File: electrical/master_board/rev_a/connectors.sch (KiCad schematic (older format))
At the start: 9 parts, among them CN3 LIDAR_ADAPTER;2xF1x2, CN40 MIKROBUS_MATE;SMALL, CN41 MIKROBUS_MATE;MEDIUM, U10 SN74HCS595;TTSOP16, U11 SN74HCS166;TTSOP16, U12 SN74HCS166;TTSOP16

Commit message: Reannoted. Postioned components are in the 80-99 reference range.
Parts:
- renumbered C18 to C14, C19 to C15, C20 to C16, CN3 to CN5, CN40 to CN88, CN41 to CN89, U10 to U5, U11 to U6, U12 to U7
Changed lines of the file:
@@
 P 4500 4100
 AR Path="/5F4CFB97" Ref="CN?"  Part="1"
-AR Path="/5F4CEE66/5F4CFB97" Ref="CN40"  Part="1"
-F 0 "CN40" H 4800 4250 50  0000 C CNN
+AR Path="/5F4CEE66/5F4CFB97" Ref="CN88"  Part="1"
+F 0 "CN88" H 4800 4250 50  0000 C CNN
 F 1 "MIKROBUS_MATE;SMALL" H 5050 2850 50  0000 C CNN
 F 2 "HR2:MIKROBUS_SMALL_MATE" H 4700 4150 60  0001 L CNN
@@
 P 4500 2500
 AR Path="/5F4CFB9E" Ref="CN?"  Part="1"
-AR Path="/5F4CEE66/5F4CFB9E" Ref="CN41"  Part="1"
-F 0 "CN41" H 4800 2650 50  0000 C CNN
+AR Path="/5F4CEE66/5F4CFB9E" Ref="CN89"  Part="1"
+F 0 "CN89" H 4800 2650 50  0000 C CNN
 F 1 "MIKROBUS_MATE;MEDIUM" H 5050 1250 50  0000 C CNN
 F 2 "HR2:MIKROBUS_MEDIUM_MATE" H 4700 2550 60  0001 L CNN
@@
 ~DIO_NSS
 $Comp
-L HR2:SN74HCS595;TTSOP16 U10
+L HR2:SN74HCS595;TTSOP16 U5
 U 1 1 5FD710B8
 P 2800 6400
-F 0 "U10" H 3050 6550 50  0000 C CNN
+F 0 "U5" H 3050 6550 50  0000 C CNN
 F 1 "SN74HCS595;TTSOP16" H 3300 5250 50  0000 C CNN
 F 2 "Package_SO:TSSOP-16_4.4x5mm_P0.65mm" H 3000 6450 60  0001 L CNN
@@
 P 4600 5700
 AR Path="/5F4A826A/5F84DF13" Ref="CN?"  Part="1"
-AR Path="/5F4CEE66/5F84DF13" Ref="CN3"  Part="1"
-F 0 "CN3" H 4850 5850 50  0000 C CNN
+AR Path="/5F4CEE66/5F84DF13" Ref="CN5"  Part="1"
+F 0 "CN5" H 4850 5850 50  0000 C CNN
 F 1 "LIDAR_ADAPTER;2xF1x2" H 5100 5150 50  0000 C CNN
 F 2 "HR2:LIDAR_ADAPTER_2xF1x2" H 4800 5750 60  0001 L CNN
@@
 	5900 5500 6000 5600
 $Comp
-L HR2:SN74HCS166;TTSOP16 U11
+L HR2:SN74HCS166;TTSOP16 U6
 U 1 1 5F845F8F
 P 8300 2500
-F 0 "U11" H 8550 2650 60  0000 C CNN
+F 0 "U6" H 8550 2650 60  0000 C CNN
 F 1 "SN74HCS166;TTSOP16" H 8900 1150 60  0000 C CNN
 F 2 "Package_SO:TSSOP-16_4.4x5mm_P0.65mm" H 8500 2550 60  0001 L CNN
@@
 $EndComp
 $Comp
-L HR2:SN74HCS166;TTSOP16 U12
+L HR2:SN74HCS166;TTSOP16 U7
 U 1 1 5F849624
 P 8300 4700
-F 0 "U12" H 8550 4850 60  0000 C CNN
+F 0 "U7" H 8550 4850 60  0000 C CNN
 F 1 "SN74HCS166;TTSOP16" H 8900 3350 60  0000 C CNN
 F 2 "Package_SO:TSSOP-16_4.4x5mm_P0.65mm" H 8500 4750 60  0001 L CNN
@@
 P 4600 1750
 AR Path="/5F48CAAD/5F97D822" Ref="C?"  Part="1"
-AR Path="/5F4CEE66/5F97D822" Ref="C18"  Part="1"
-F 0 "C18" H 4400 1850 50  0000 L CNN
+AR Path="/5F4CEE66/5F97D822" Ref="C14"  Part="1"
+F 0 "C14" H 4400 1850 50  0000 L CNN
 F 1 "10pF;1608" H 4650 1650 50  0000 L CNN
 F 2 "" H 4638 1600 50  0001 C CNN
@@
 P 5200 1750
 AR Path="/5F48CAAD/5F97D82E" Ref="C?"  Part="1"
-AR Path="/5F4CEE66/5F97D82E" Ref="C19"  Part="1"
-F 0 "C19" H 5000 1850 50  0000 L CNN
+AR Path="/5F4CEE66/5F97D82E" Ref="C15"  Part="1"
+F 0 "C15" H 5000 1850 50  0000 L CNN
 F 1 "10pF;1608" H 5250 1650 50  0000 L CNN
 F 2 "" H 5238 1600 50  0001 C CNN
@@
 P 5800 1750
 AR Path="/5F48CAAD/5F97D834" Ref="C?"  Part="1"
-AR Path="/5F4CEE66/5F97D834" Ref="C20"  Part="1"
-F 0 "C20" H 5600 1850 50  0000 L CNN
+AR Path="/5F4CEE66/5F97D834" Ref="C16"  Part="1"
+F 0 "C16" H 5600 1850 50  0000 L CNN
 F 1 "10pF;1608" H 5850 1650 50  0000 L CNN
 F 2 "" H 5838 1600 50  0001 C CNN

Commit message: Assigned PCB footprints.
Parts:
- C14, C15, C16: footprint (none) -> Capacitor_SMD:C_0603_1608Metric
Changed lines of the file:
@@
 F 0 "C14" H 4400 1850 50  0000 L CNN
 F 1 "10pF;1608" H 4650 1650 50  0000 L CNN
-F 2 "" H 4638 1600 50  0001 C CNN
+F 2 "Capacitor_SMD:C_0603_1608Metric" H 4638 1600 50  0001 C CNN
 F 3 "~" H 4600 1750 50  0001 C CNN
 	1    4600 1750
@@
 F 0 "C15" H 5000 1850 50  0000 L CNN
 F 1 "10pF;1608" H 5250 1650 50  0000 L CNN
-F 2 "" H 5238 1600 50  0001 C CNN
+F 2 "Capacitor_SMD:C_0603_1608Metric" H 5238 1600 50  0001 C CNN
 F 3 "~" H 5200 1750 50  0001 C CNN
 	1    5200 1750
@@
 F 0 "C16" H 5600 1850 50  0000 L CNN
 F 1 "10pF;1608" H 5850 1650 50  0000 L CNN
-F 2 "" H 5838 1600 50  0001 C CNN
+F 2 "Capacitor_SMD:C_0603_1608Metric" H 5838 1600 50  0001 C CNN
 F 3 "~" H 5800 1750 50  0001 C CNN
 	1    5800 1750

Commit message: Imported footprints to PCB.
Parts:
- CN5: footprint HR2:LIDAR_ADAPTER_2xF1x2 -> HR2:LIDAR_ADAPTER_2xF1x2+Fx3
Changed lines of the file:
@@
 F 0 "CN5" H 4850 5850 50  0000 C CNN
 F 1 "LIDAR_ADAPTER;2xF1x2" H 5100 5150 50  0000 C CNN
-F 2 "HR2:LIDAR_ADAPTER_2xF1x2" H 4800 5750 60  0001 L CNN
+F 2 "HR2:LIDAR_ADAPTER_2xF1x2+Fx3" H 4800 5750 60  0001 L CNN
 F 3 "Lidar Adapter Connectors" H 4800 5550 60  0001 L CNN
 F 4 "Lidar Adapter Connectors" H 4800 5650 60  0001 L CNN "manf#"

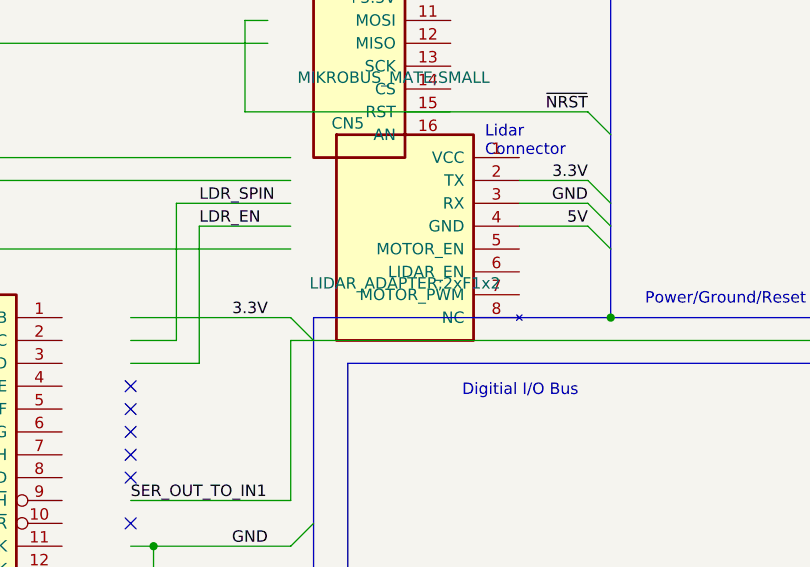
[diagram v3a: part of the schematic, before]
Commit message: Postioned all the components properly.
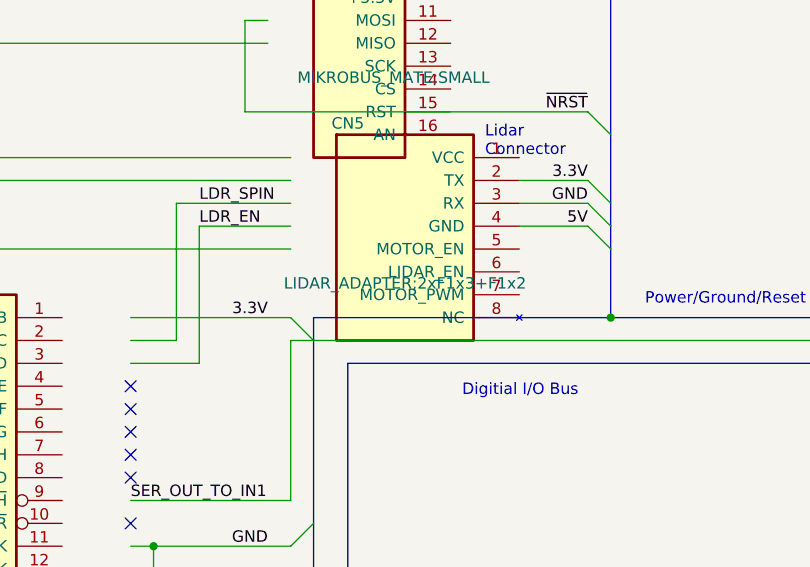
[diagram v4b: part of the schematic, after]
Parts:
- CN5: value LIDAR_ADAPTER;2xF1x2 -> LIDAR_ADAPTER;2xF1x3+F1x2; footprint HR2:LIDAR_ADAPTER_2xF1x2+Fx3 -> HR2:LIDAR_ADAPTER_2xF1x3+F1x2
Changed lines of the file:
@@
 AR Path="/5F4CEE66/5F84DF13" Ref="CN5"  Part="1"
 F 0 "CN5" H 4850 5850 50  0000 C CNN
-F 1 "LIDAR_ADAPTER;2xF1x2" H 5100 5150 50  0000 C CNN
-F 2 "HR2:LIDAR_ADAPTER_2xF1x2+Fx3" H 4800 5750 60  0001 L CNN
+F 1 "LIDAR_ADAPTER;2xF1x3+F1x2" H 5100 5150 50  0000 C CNN
+F 2 "HR2:LIDAR_ADAPTER_2xF1x3+F1x2" H 4800 5750 60  0001 L CNN
 F 3 "Lidar Adapter Connectors" H 4800 5550 60  0001 L CNN
 F 4 "Lidar Adapter Connectors" H 4800 5650 60  0001 L CNN "manf#"

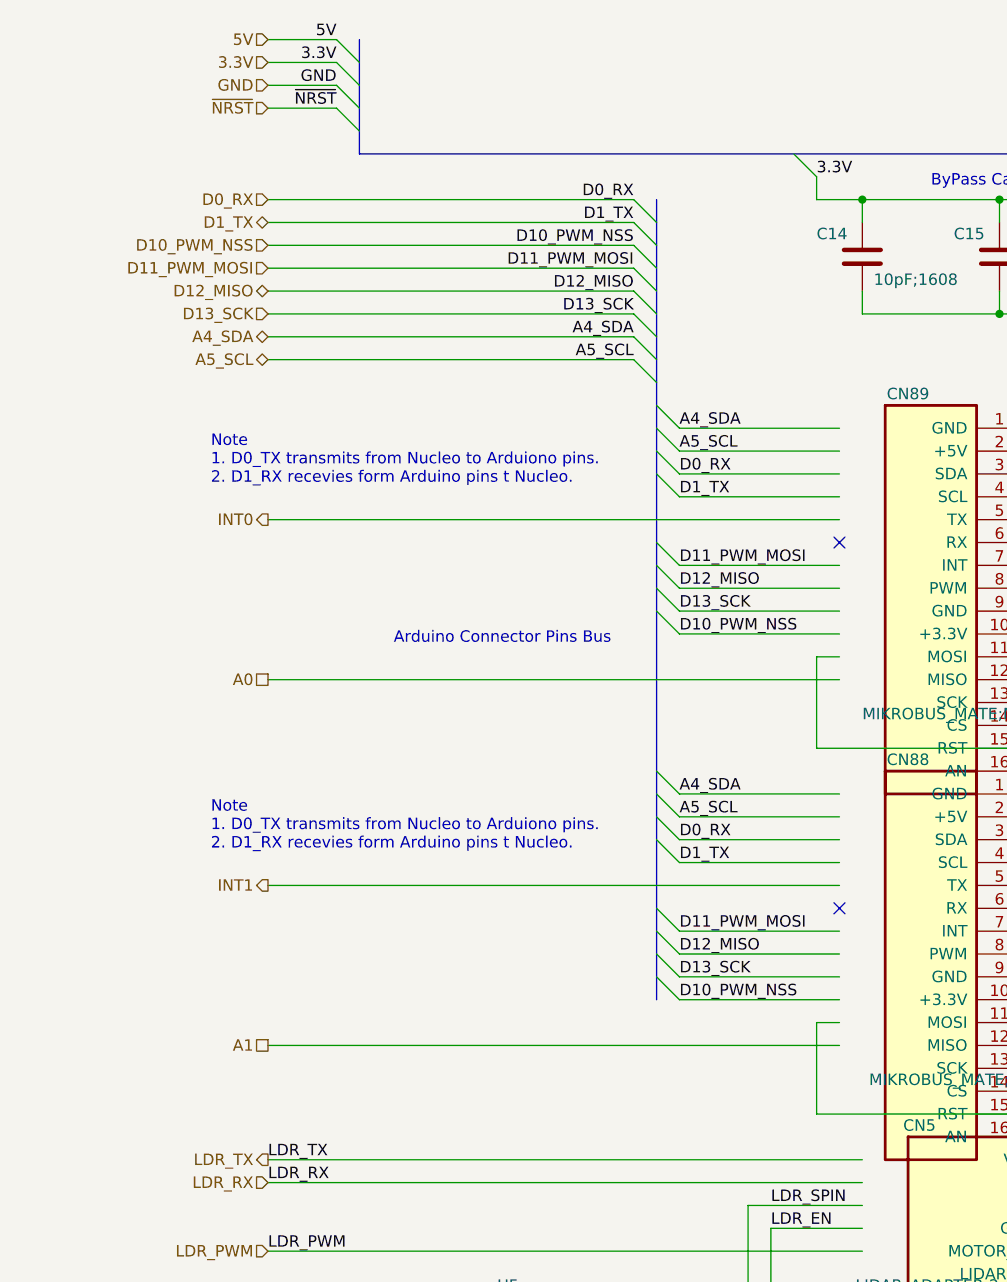
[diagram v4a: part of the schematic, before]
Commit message: Weaving traces from NE corner around the heat sink holes.
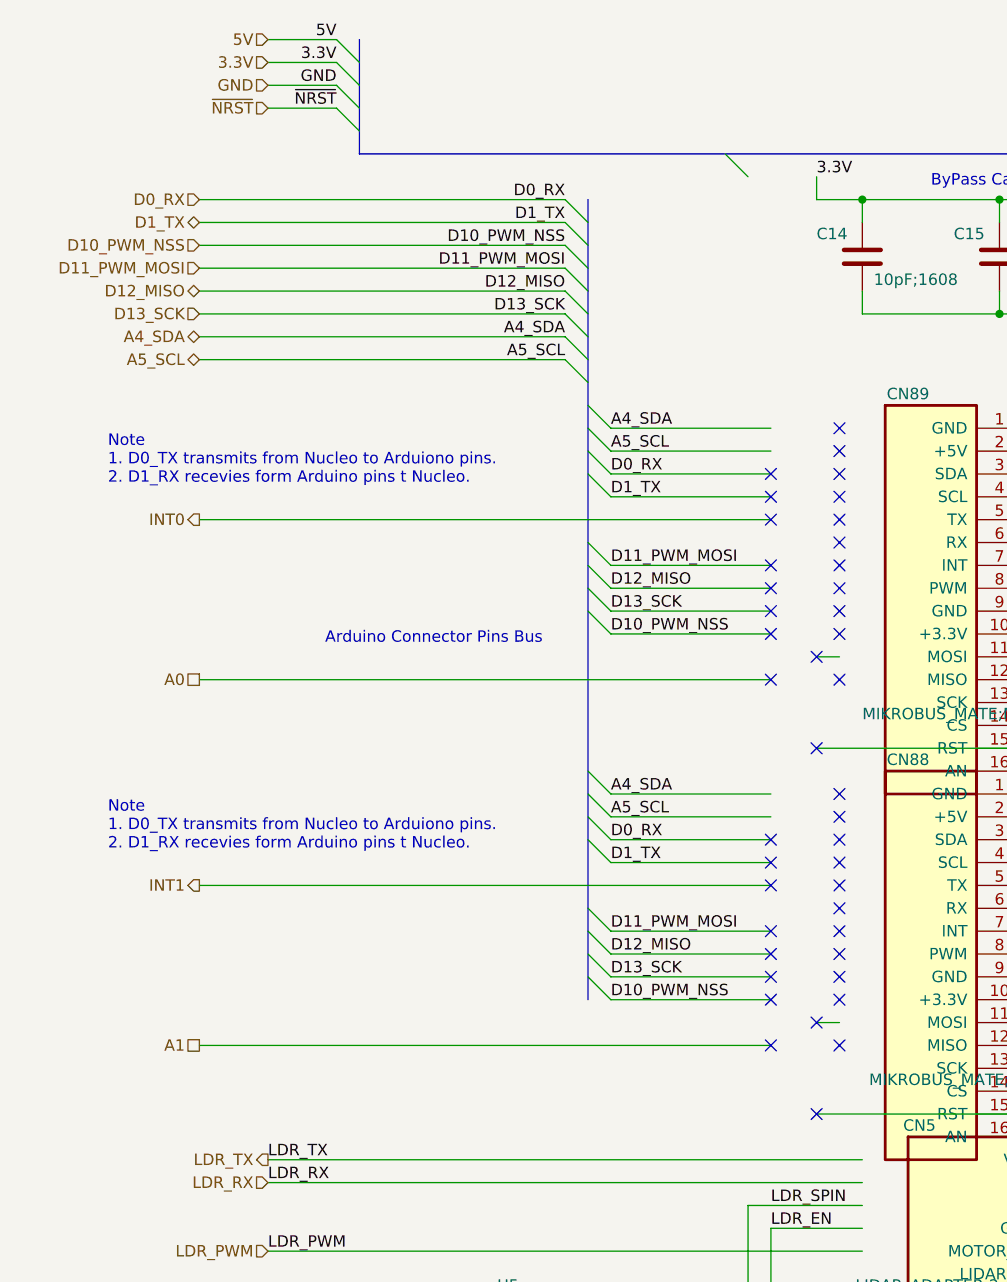
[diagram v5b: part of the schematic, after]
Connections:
- wire segments 157 -> 155
- no-connect marks 8 -> 48
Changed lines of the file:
@@
 Wire Wire Line
 	3900 6400 4600 6400
-Text HLabel 2000 3600 0    50   UnSpc ~ 0
+Text HLabel 1700 3600 0    50   UnSpc ~ 0
 A0
-Text HLabel 2000 5200 0    50   UnSpc ~ 0
+Text HLabel 1700 5200 0    50   UnSpc ~ 0
 A1
 Text HLabel 2000 1100 0    50   Input ~ 0
 ~NRST
-Text HLabel 2000 2200 0    50   BiDi ~ 0
+Text HLabel 1700 2200 0    50   BiDi ~ 0
 A5_SCL
-Text HLabel 2000 2100 0    50   BiDi ~ 0
+Text HLabel 1700 2100 0    50   BiDi ~ 0
 A4_SDA
-Text HLabel 2000 2000 0    50   Input ~ 0
+Text HLabel 1700 2000 0    50   Input ~ 0
 D13_SCK
-Text HLabel 2000 1900 0    50   BiDi ~ 0
+Text HLabel 1700 1900 0    50   BiDi ~ 0
 D12_MISO
-Text HLabel 2000 1800 0    50   Input ~ 0
+Text HLabel 1700 1800 0    50   Input ~ 0
 D11_PWM_MOSI
-Text HLabel 2000 1700 0    50   Input ~ 0
+Text HLabel 1700 1700 0    50   Input ~ 0
 D10_PWM_NSS
-Text HLabel 2000 1600 0    50   BiDi ~ 0
+Text HLabel 1700 1600 0    50   BiDi ~ 0
 D1_TX
-Text HLabel 2000 1500 0    50   Input ~ 0
+Text HLabel 1700 1500 0    50   Input ~ 0
 D0_RX
-Text Label 3600 1800 2    50   ~ 0
+Text Label 3300 1800 2    50   ~ 0
 D11_PWM_MOSI
 Entry Wire Line
-	3700 3000 3800 3100
+	3400 3000 3500 3100
 NoConn ~ 4500 3000
 Entry Wire Line
-	3700 3100 3800 3200
-Entry Wire Line
-	3700 3200 3800 3300
-Entry Wire Line
-	3700 3300 3800 3400
-Entry Wire Line
-	3700 2400 3800 2500
-Entry Wire Line
-	3700 2500 3800 2600
-Entry Wire Line
-	3700 2600 3800 2700
-Entry Wire Line
-	3800 2800 3700 2700
-Entry Wire Line
-	3600 2000 3700 2100
-Entry Wire Line
-	3600 2100 3700 2200
-Entry Wire Line
-	3600 2200 3700 2300
+	3400 3100 3500 3200
+Entry Wire Line
+	3400 3200 3500 3300
+Entry Wire Line
+	3400 3300 3500 3400
+Entry Wire Line
+	3400 2400 3500 2500
+Entry Wire Line
+	3400 2500 3500 2600
+Entry Wire Line
+	3400 2600 3500 2700
+Entry Wire Line
+	3500 2800 3400 2700
+Entry Wire Line
+	3300 2000 3400 2100
+Entry Wire Line
+	3300 2100 3400 2200
+Entry Wire Line
+	3300 2200 3400 2300
 Entry Wire Line
 	2300 1100 2400 1200
 Entry Wire Line
-	3600 1500 3700 1600
-Entry Wire Line
-	3600 1600 3700 1700
-Entry Wire Line
-	3600 1700 3700 1800
-Entry Wire Line
-	3700 1900 3600 1800
-Entry Wire Line
-	3600 1900 3700 2000
-Text Label 3600 1700 2    50   ~ 0
+	3300 1500 3400 1600
+Entry Wire Line
+	3300 1600 3400 1700
+Entry Wire Line
+	3300 1700 3400 1800
+Entry Wire Line
+	3400 1900 3300 1800
+Entry Wire Line
+	3300 1900 3400 2000
+Text Label 3300 1700 2    50   ~ 0
 D10_PWM_NSS
-Text Label 3600 1600 2    50   ~ 0
+Text Label 3300 1600 2    50   ~ 0
 D1_TX
-Text Label 3600 1500 2    50   ~ 0
+Text Label 3300 1500 2    50   ~ 0
 D0_RX
-Text Label 3600 1900 2    50   ~ 0
+Text Label 3300 1900 2    50   ~ 0
 D12_MISO
-Text Label 3600 2000 2    50   ~ 0
+Text Label 3300 2000 2    50   ~ 0
 D13_SCK
-Text Label 3600 2100 2    50   ~ 0
+Text Label 3300 2100 2    50   ~ 0
 A4_SDA
-Text Label 3600 2200 2    50   ~ 0
+Text Label 3300 2200 2    50   ~ 0
 A5_SCL
 Text Label 2300 1100 2    50   ~ 0
 ~NRST
-Text Label 3800 3100 0    50   ~ 0
+Text Label 3500 3100 0    50   ~ 0
 D11_PWM_MOSI
-Text Label 3800 2800 0    50   ~ 0
+Text Label 3500 2800 0    50   ~ 0
 D1_TX
-Text Label 3800 2700 0    50   ~ 0
+Text Label 3500 2700 0    50   ~ 0
 D0_RX
-Text Label 3800 3200 0    50   ~ 0
+Text Label 3500 3200 0    50   ~ 0
 D12_MISO
-Text Label 3800 3300 0    50   ~ 0
+Text Label 3500 3300 0    50   ~ 0
 D13_SCK
-Text Label 3800 2500 0    50   ~ 0
+Text Label 3500 2500 0    50   ~ 0
 A4_SDA
-Text Label 3800 2600 0    50   ~ 0
+Text Label 3500 2600 0    50   ~ 0
 A5_SCL
 Wire Wire Line
-	2000 1500 3600 1500
-Wire Wire Line
-	3600 1600 2000 1600
-Wire Wire Line
-	2000 1700 3600 1700
-Wire Wire Line
-	3600 1800 2000 1800
-Wire Wire Line
-	2000 1900 3600 1900
-Wire Wire Line
-	3600 2000 2000 2000
-Wire Wire Line
-	2000 2100 3600 2100
-Wire Wire Line
-	3600 2200 2000 2200
+	1700 1500 3300 1500
+Wire Wire Line
+	3300 1600 1700 1600
+Wire Wire Line
+	1700 1700 3300 1700
+Wire Wire Line
+	3300 1800 1700 1800
+Wire Wire Line
+	1700 1900 3300 1900
+Wire Wire Line
+	3300 2000 1700 2000
+Wire Wire Line
+	1700 2100 3300 2100
+Wire Wire Line
+	3300 2200 1700 2200
 Wire Wire Line
 	2000 1100 2300 1100
 Wire Wire Line
-	4500 2500 3800 2500
-Wire Wire Line
-	3800 2600 4500 2600
-Wire Wire Line
-	4500 2700 3800 2700
-Wire Wire Line
-	3800 2800 4500 2800
-Wire Wire Line
-	4500 3100 3800 3100
-Wire Wire Line
-	3800 3200 4500 3200
-Wire Wire Line
-	4500 3300 3800 3300
-Wire Wire Line
-	3800 3400 4500 3400
+	4200 2500 3500 2500
+Wire Wire Line
+	3500 2600 4200 2600
+Wire Wire Line
+	4200 2700 3500 2700
+Wire Wire Line
+	3500 2800 4200 2800
+Wire Wire Line
+	4200 3100 3500 3100
+Wire Wire Line
+	3500 3200 4200 3200
+Wire Wire Line
+	4200 3300 3500 3300
+Wire Wire Line
+	3500 3400 4200 3400
 Wire Wire Line
 	4500 3500 4400 3500
 Wire Wire Line
-	4500 2900 2000 2900
-Entry Wire Line
-	3700 4600 3800 4700
-Entry Wire Line
-	3700 4700 3800 4800
-Entry Wire Line
-	3700 4800 3800 4900
-Entry Wire Line
-	3700 4900 3800 5000
-Entry Wire Line
-	3700 4000 3800 4100
-Entry Wire Line
-	3700 4100 3800 4200
-Entry Wire Line
-	3700 4200 3800 4300
-Entry Wire Line
-	3800 4400 3700 4300
-Text Label 3800 4700 0    50   ~ 0
+	4200 2900 1700 2900
+Entry Wire Line
+	3400 4600 3500 4700
+Entry Wire Line
+	3400 4700 3500 4800
+Entry Wire Line
+	3400 4800 3500 4900
+Entry Wire Line
+	3400 4900 3500 5000
+Entry Wire Line
+	3400 4000 3500 4100
+Entry Wire Line
+	3400 4100 3500 4200
+Entry Wire Line
+	3400 4200 3500 4300
+Entry Wire Line
+	3500 4400 3400 4300
+Text Label 3500 4700 0    50   ~ 0
 D11_PWM_MOSI
-Text Label 3800 5000 0    50   ~ 0
+Text Label 3500 5000 0    50   ~ 0
 D10_PWM_NSS
-Text Label 3800 4400 0    50   ~ 0
+Text Label 3500 4400 0    50   ~ 0
 D1_TX
-Text Label 3800 4300 0    50   ~ 0
+Text Label 3500 4300 0    50   ~ 0
 D0_RX
-Text Label 3800 4800 0    50   ~ 0
+Text Label 3500 4800 0    50   ~ 0
 D12_MISO
-Text Label 3800 4900 0    50   ~ 0
+Text Label 3500 4900 0    50   ~ 0
 D13_SCK
-Text Label 3800 4100 0    50   ~ 0
+Text Label 3500 4100 0    50   ~ 0
 A4_SDA
-Text Label 3800 4200 0    50   ~ 0
+Text Label 3500 4200 0    50   ~ 0
 A5_SCL
 Text Label 5900 5500 2    50   ~ 0
 ~NRST
 Wire Wire Line
-	4500 4100 3800 4100
-Wire Wire Line
-	3800 4200 4500 4200
-Wire Wire Line
-	4500 4300 3800 4300
-Wire Wire Line
-	3800 4400 4500 4400
-Wire Wire Line
-	4500 4700 3800 4700
-Wire Wire Line
-	3800 4800 4500 4800
-Wire Wire Line
-	4500 4900 3800 4900
-Wire Wire Line
-	3800 5000 4500 5000
-Wire Wire Line
-	4500 4500 2000 4500
-Wire Wire Line
-	2000 3600 4500 3600
-Wire Wire Line
-	2000 5200 4500 5200
-Text HLabel 2000 4500 0    50   Output ~ 0
+	4200 4100 3500 4100
+Wire Wire Line
+	3500 4200 4200 4200
+Wire Wire Line
+	4200 4300 3500 4300
+Wire Wire Line
+	3500 4400 4200 4400
+Wire Wire Line
+	4200 4700 3500 4700
+Wire Wire Line
+	3500 4800 4200 4800
+Wire Wire Line
+	4200 4900 3500 4900
+Wire Wire Line
+	3500 5000 4200 5000
+Wire Wire Line
+	4200 4500 1700 4500
+Wire Wire Line
+	1700 3600 4200 3600
+Wire Wire Line
+	1700 5200 4200 5200
+Text HLabel 1700 4500 0    50   Output ~ 0
 INT1
-Text HLabel 2000 2900 0    50   Output ~ 0
+Text HLabel 1700 2900 0    50   Output ~ 0
 INT0
 NoConn ~ 4500 4600
@@
 ~NRST
 Wire Wire Line
-	4400 3500 4400 3900
-Wire Wire Line
 	4400 3900 5900 3900
 Entry Wire Line
@@
 Wire Wire Line
 	4500 5100 4400 5100
-Wire Wire Line
-	4400 5100 4400 5500
 Wire Wire Line
 	4400 5500 5900 5500
@@
 Text Notes 2400 6550 0    50   ~ 0
 8-Bit Parallel\nto Serial\nShift Register
-Text Label 3800 3400 0    50   ~ 0
+Text Label 3500 3400 0    50   ~ 0
 D10_PWM_NSS
 Text Label 1500 7450 0    50   ~ 0
 DIO_SCK
-Text Notes 2550 3450 0    50   ~ 0
+Text Notes 2250 3450 0    50   ~ 0
 Arduino Connector Pins Bus
 Wire Wire Line
@@
 Text Notes 6550 4150 0    50   ~ 0
 Digitial I/O Bus
-Text Notes 1750 2750 0    50   ~ 0
+Text Notes 1300 2750 0    50   ~ 0
 Note\n1. D0_TX transmits from Nucleo to Arduiono pins.\n2. D1_RX recevies form Arduino pins t Nucleo.
-Text Notes 1750 4350 0    50   ~ 0
+Text Notes 1300 4350 0    50   ~ 0
 Note\n1. D0_TX transmits from Nucleo to Arduiono pins.\n2. D1_RX recevies form Arduino pins t Nucleo.
 Text Label 4400 1400 0    50   ~ 0
@@
 	4600 1900 4600 2000
 Entry Wire Line
-	4400 1400 4300 1300
+	4100 1400 4000 1300
 Entry Wire Line
 	6300 1400 6200 1300
@@
 Text Notes 7200 1550 0    50   ~ 0
 Note: There are many extra input pins.  Most of these will be assigned\nto Grove connectors and edge detectors.
+NoConn ~ 4500 2500
+NoConn ~ 4500 2600
+NoConn ~ 4500 2700
+NoConn ~ 4500 2800
+NoConn ~ 4500 2900
+NoConn ~ 4500 3100
+NoConn ~ 4500 3200
+NoConn ~ 4500 3300
+NoConn ~ 4500 3400
+NoConn ~ 4500 3600
+NoConn ~ 4200 2700
+NoConn ~ 4200 2800
+NoConn ~ 4200 2900
+NoConn ~ 4200 3100
+NoConn ~ 4200 3200
+NoConn ~ 4200 3300
+NoConn ~ 4200 3400
+NoConn ~ 4200 3600
+NoConn ~ 4200 5200
+NoConn ~ 4500 5200
+NoConn ~ 4500 5000
+NoConn ~ 4500 4900
+NoConn ~ 4500 4800
+NoConn ~ 4500 4700
+NoConn ~ 4500 4500
+NoConn ~ 4500 4400
+NoConn ~ 4500 4300
+NoConn ~ 4500 4200
+NoConn ~ 4500 4100
+NoConn ~ 4200 4300
+NoConn ~ 4200 4400
+NoConn ~ 4200 4500
+NoConn ~ 4200 4700
+NoConn ~ 4200 4800
+NoConn ~ 4200 4900
+NoConn ~ 4200 5000
+NoConn ~ 4400 3500
+NoConn ~ 4400 3900
+NoConn ~ 4400 5100
+NoConn ~ 4400 5500
 Wire Wire Line
 	4600 6500 8100 6500
@@
 	6000 2900 6000 6400
 Wire Bus Line
-	3700 1500 3700 5000
+	3400 1500 3400 5000
 $EndSCHEMATC

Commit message: Continue to work on PCB's.
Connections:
- wire segments 155 -> 157
- no-connect marks 48 -> 44
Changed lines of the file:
@@
 ~NRST
 Wire Wire Line
-	4400 3900 5900 3900
-Entry Wire Line
-	5900 3900 6000 4000
-Text Label 5900 3900 2    50   ~ 0
-~NRST
-Wire Wire Line
 	4500 5100 4400 5100
-Wire Wire Line
-	4400 5500 5900 5500
 Entry Wire Line
 	5900 5500 6000 5600
@@
 NoConn ~ 4200 4900
 NoConn ~ 4200 5000
-NoConn ~ 4400 3500
-NoConn ~ 4400 3900
-NoConn ~ 4400 5100
-NoConn ~ 4400 5500
+Wire Wire Line
+	4400 5500 5900 5500
+Entry Wire Line
+	5900 3900 6000 4000
+Text Label 5900 3900 2    50   ~ 0
+~NRST
+Wire Wire Line
+	4400 3900 5900 3900
+Wire Wire Line
+	4400 3900 4400 3500
+Wire Wire Line
+	4400 5500 4400 5100
 Wire Wire Line
 	4600 6500 8100 6500
